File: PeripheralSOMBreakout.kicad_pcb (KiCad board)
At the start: 2 copper layers, 61.8 x 79.5 mm, 13 parts, among them J1 53307-2471, J2 24V, J3 GND, J4 Digital A, J5 Digital B, J6 Analog

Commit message: finished
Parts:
- moved TP2 8.00 mm to (146.2, 68.8)
- moved TP3 8.00 mm to (151.2, 62.5)
- moved LOGO1 1.50 mm to (118.8, 133.0)
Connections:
- J4 pad 1: /CAN_H -> /I2C1_SDA
- J4 pad 2: /CAN_L -> /I2C1_SCL
- J4 pad 3: /I2C1_SDA -> /CAN_L
- J4 pad 4: /I2C1_SCL -> /CAN_H
- J5 pad 2: /SPI2_MOSI -> /SPI2_NSS
- J5 pad 4: /SPI2_NSS -> /SPI2_MOSI
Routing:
- net /ADC1_IN11: track 0.00 -> 62.6 mm, vias 0 -> 1
- net /ADC1_IN10: track 0.00 -> 60.3 mm, vias 0 -> 1
- net /OPAMP1_VINP: track 0.00 -> 59.1 mm, vias 0 -> 1
- net /ADC1_IN9: track 0.00 -> 58.1 mm, vias 0 -> 1
- net /ADC1_IN7: track 0.00 -> 57.7 mm, vias 0 -> 1
- net /SPI2_MISO: track 0.00 -> 48.1 mm, vias 0 -> 1
- net /SPI2_NSS: track 0.00 -> 46.3 mm, vias 0 -> 1
- net /SPI2_SCK: track 0.00 -> 44.7 mm, vias 0 -> 1
- net /SPI2_MOSI: track 0.00 -> 43.0 mm, vias 0 -> 1
- net /I2C1_SDA: track 0.00 -> 42.5 mm
- net /I2C1_SCL: track 0.00 -> 36.2 mm
- net /SPI1_MISO: track 0.00 -> 33.2 mm, vias 0 -> 1
- net /CAN_L: track 0.00 -> 32.2 mm
- net /SPI1_SCK: track 0.00 -> 32.2 mm, vias 0 -> 1
- net +3.3V: track 0.00 -> 32.2 mm, vias 0 -> 1
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- added copper zone on F.Cu, net +24V
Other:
- board size 61.8 x 79.5 mm -> 61.8 x 81.1 mm
- board text added: "AMP"
- board text added: "CAN_H"
- board text added: "CAN_L"
- board text added: "I2C1"
- board text added: "IN10"
- board text added: "IN11"
- board text added: "IN7"
- board text added: "IN9"
- board text added: "MCU PWR"
- board text added: "MISO"
- board text added: "MOSI"
- board text added: "NSS"
- board text added: "SCK"
- board text added: "SCL"
- board text added: "SDA"
- board text added: "SPI1"
- board text added: "SPI2"
- board text added: "label every pin"

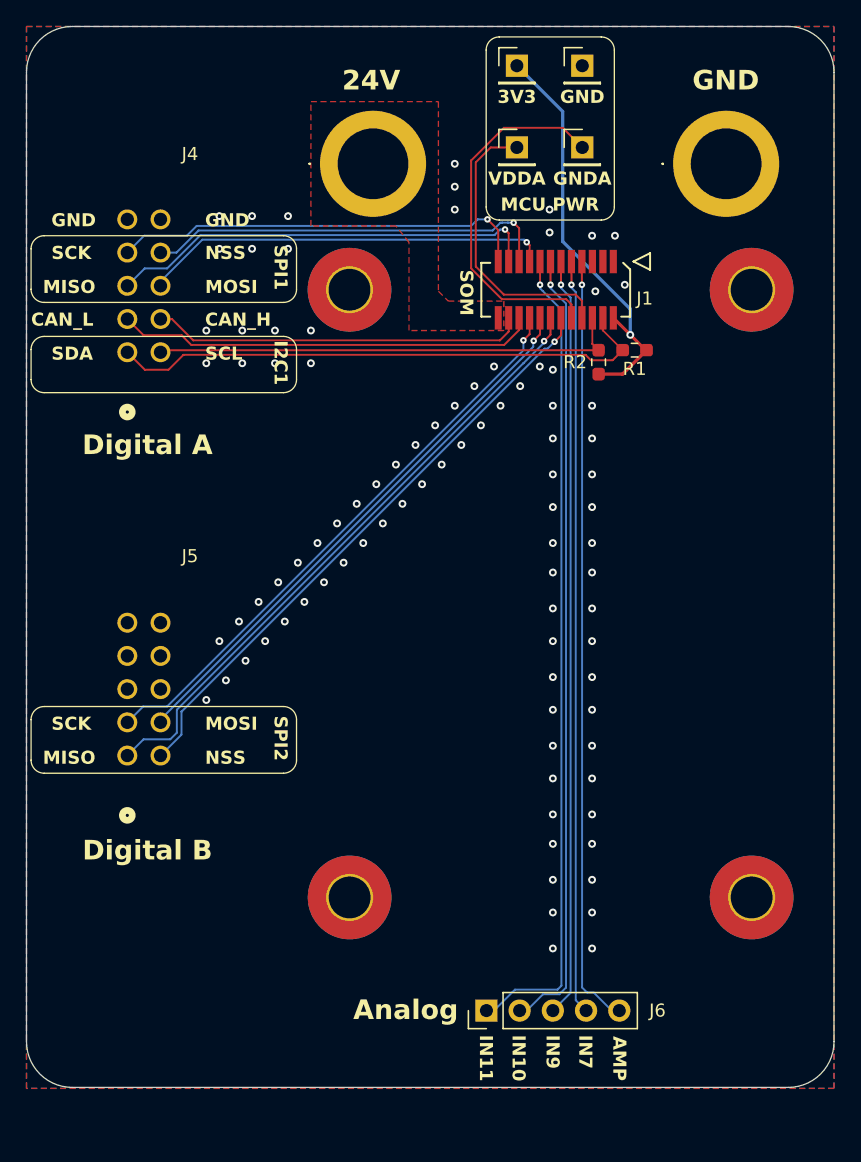
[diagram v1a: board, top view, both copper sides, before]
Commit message: add db9 for can
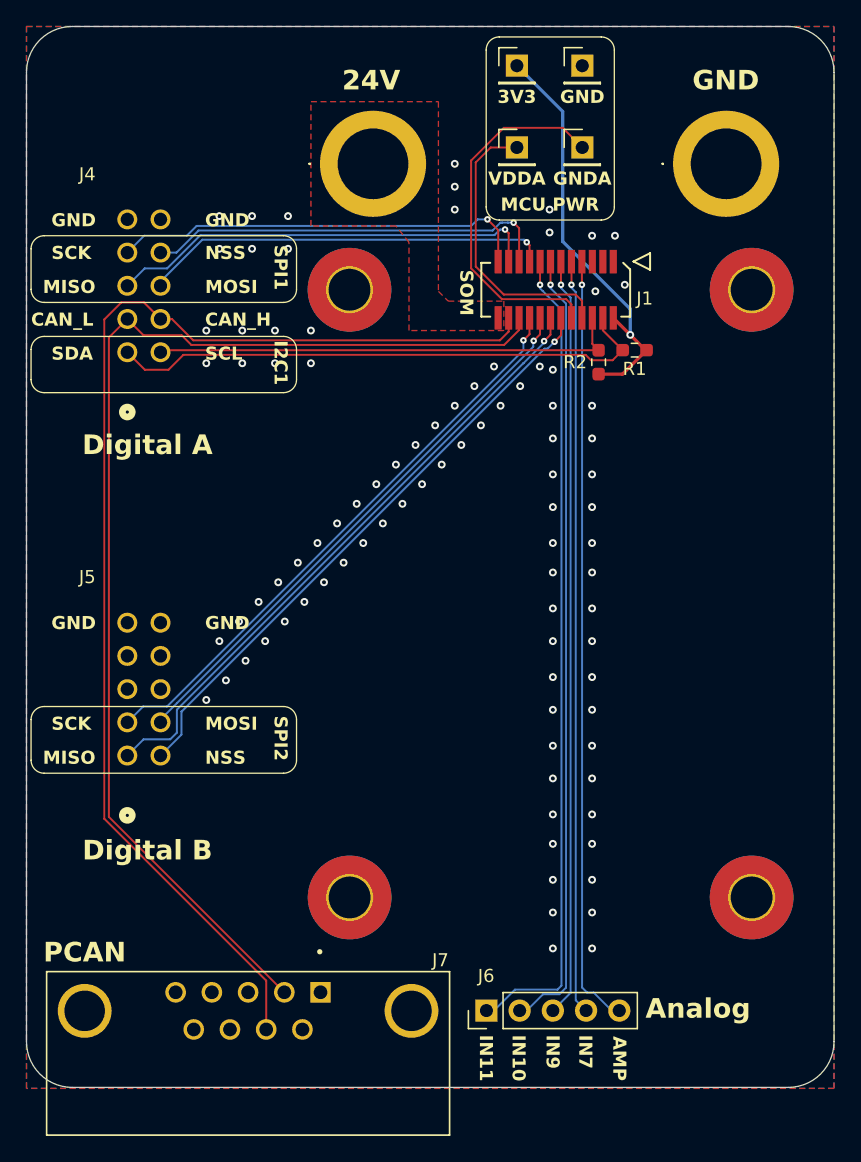
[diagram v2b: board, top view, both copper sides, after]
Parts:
- added J7: PCAN, DB9:AMPHENOL_L77SDE09SA4CH3R, F.Cu at (125.7, 134.8)
- moved LOGO1 69.2 mm to (118.4, 63.8)
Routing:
- net /CAN_H: track 28.6 -> 93.4 mm
- net /CAN_L: track 32.2 -> 89.8 mm
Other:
- board text removed: "label every pin"
